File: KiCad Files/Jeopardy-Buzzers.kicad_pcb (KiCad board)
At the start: 2 copper layers, 40 x 30 mm, 30 parts, among them J1 USB_C_Receptacle_USB2.0_14P, J2 Conn_01x02_Pin, J3 Conn_01x03_Socket, J4 Conn_01x03_Socket, J5 Conn_02x04_Odd_Even, U1 CH32V003FxUx, U2 CH340N, U3 NRF24L01_Breakout, U5 AMS1117-3.3, Y1 Crystal_24MHz

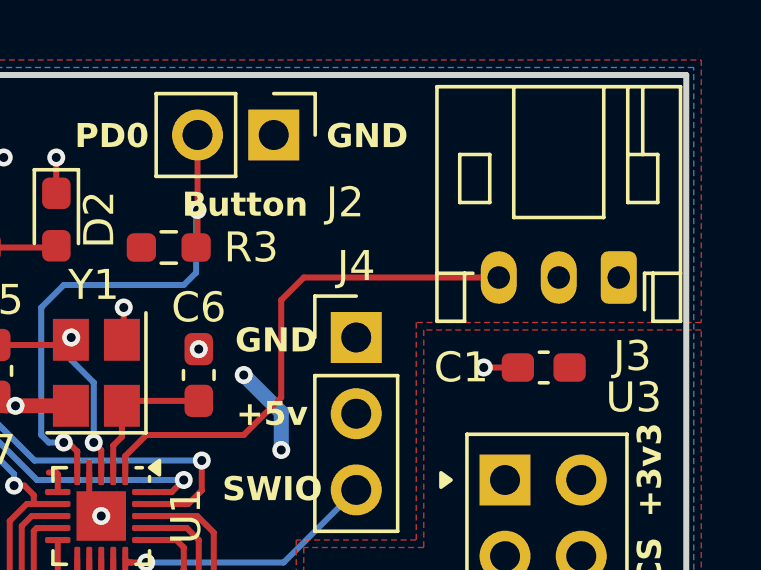
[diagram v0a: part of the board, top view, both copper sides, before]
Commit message: Had the pinout for the addressable RGB cable backwards
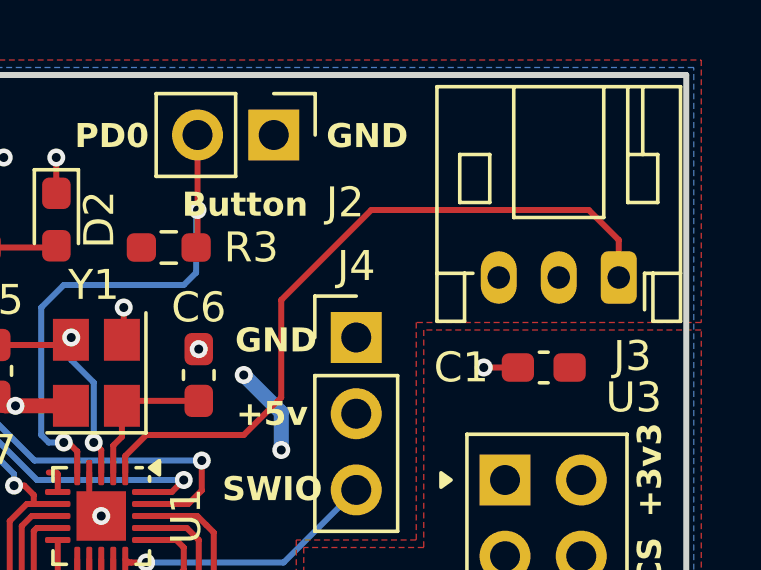
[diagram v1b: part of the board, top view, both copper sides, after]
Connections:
- J3 pad 1: GND -> WS2812_LED
- J3 pad 3: WS2812_LED -> GND
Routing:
- net WS2812_LED: track 17.4 -> 24.0 mm
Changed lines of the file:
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@@
 			(remove_unused_layers no)
 			(roundrect_rratio 0.208333)
-			(net 2 "GND")
+			(net 11 "WS2812_LED")
 			(pinfunction "Pin_1")
 			(pintype "passive")
@@
 			(layers "*.Cu" "*.Mask")
 			(remove_unused_layers no)
-			(net 11 "WS2812_LED")
+			(net 2 "GND")
 			(pinfunction "Pin_3")
 			(pintype "passive")
@@
 	)
 	(segment
+		(start 41.3 32.7)
+		(end 42 32)
+		(width 0.2)
+		(layer "F.Cu")
+		(net 11)
+	)
+	(segment
+		(start 56.75 24.5)
+		(end 57.75 25.5)
+		(width 0.2)
+		(layer "F.Cu")
+		(net 11)
+	)
+	(segment
+		(start 46.5 27.5)
+		(end 49.5 24.5)
+		(width 0.2)
+		(layer "F.Cu")
+		(net 11)
+	)
+	(segment
+		(start 57.75 25.5)
+		(end 57.75 26.75)
+		(width 0.2)
+		(layer "F.Cu")
+		(net 11)
+	)
+	(segment
+		(start 46.5 30.75)
+		(end 46.5 27.5)
+		(width 0.2)
+		(layer "F.Cu")
+		(net 11)
+	)
+	(segment
+		(start 49.5 24.5)
+		(end 56.75 24.5)
+		(width 0.2)
+		(layer "F.Cu")
+		(net 11)
+	)
+	(segment
+		(start 45.25 32)
+		(end 46.5 30.75)
+		(width 0.2)
+		(layer "F.Cu")
+		(net 11)
+	)
+	(segment
 		(start 41.3 33.25)
 		(end 41.3 32.7)
 		(width 0.2)
 		(layer "F.Cu")
-		(net 11)
-	)
-	(segment
-		(start 47.25 26.75)
-		(end 53.75 26.75)
-		(width 0.2)
-		(layer "F.Cu")
-		(net 11)
-	)
-	(segment
-		(start 46.5 30.75)
-		(end 46.5 27.5)
-		(width 0.2)
-		(layer "F.Cu")
-		(net 11)
-	)
-	(segment
-		(start 46.5 27.5)
-		(end 47.25 26.75)
-		(width 0.2)
-		(layer "F.Cu")
-		(net 11)
-	)
-	(segment
-		(start 45.25 32)
-		(end 46.5 30.75)
-		(width 0.2)
-		(layer "F.Cu")
-		(net 11)
-	)
-	(segment
-		(start 41.3 32.7)
-		(end 42 32)
-		(width 0.2)
-		(layer "F.Cu")
